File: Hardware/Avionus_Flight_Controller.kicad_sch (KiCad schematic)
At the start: 1 part

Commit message: More routing
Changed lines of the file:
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@@
       (effects (font (size 1.27 1.27)) (justify left))
     )
-    (pin "TIM4_CH2" output (at 127 154.94 180)
+    (pin "TIM4_CH2" output (at 127 157.48 180)
       (effects (font (size 1.27 1.27)) (justify left))
     )
@@
       (effects (font (size 1.27 1.27)) (justify left))
     )
-    (pin "TIM4_CH1" output (at 127 157.48 180)
+    (pin "TIM4_CH1" output (at 127 154.94 180)
       (effects (font (size 1.27 1.27)) (justify left))
     )

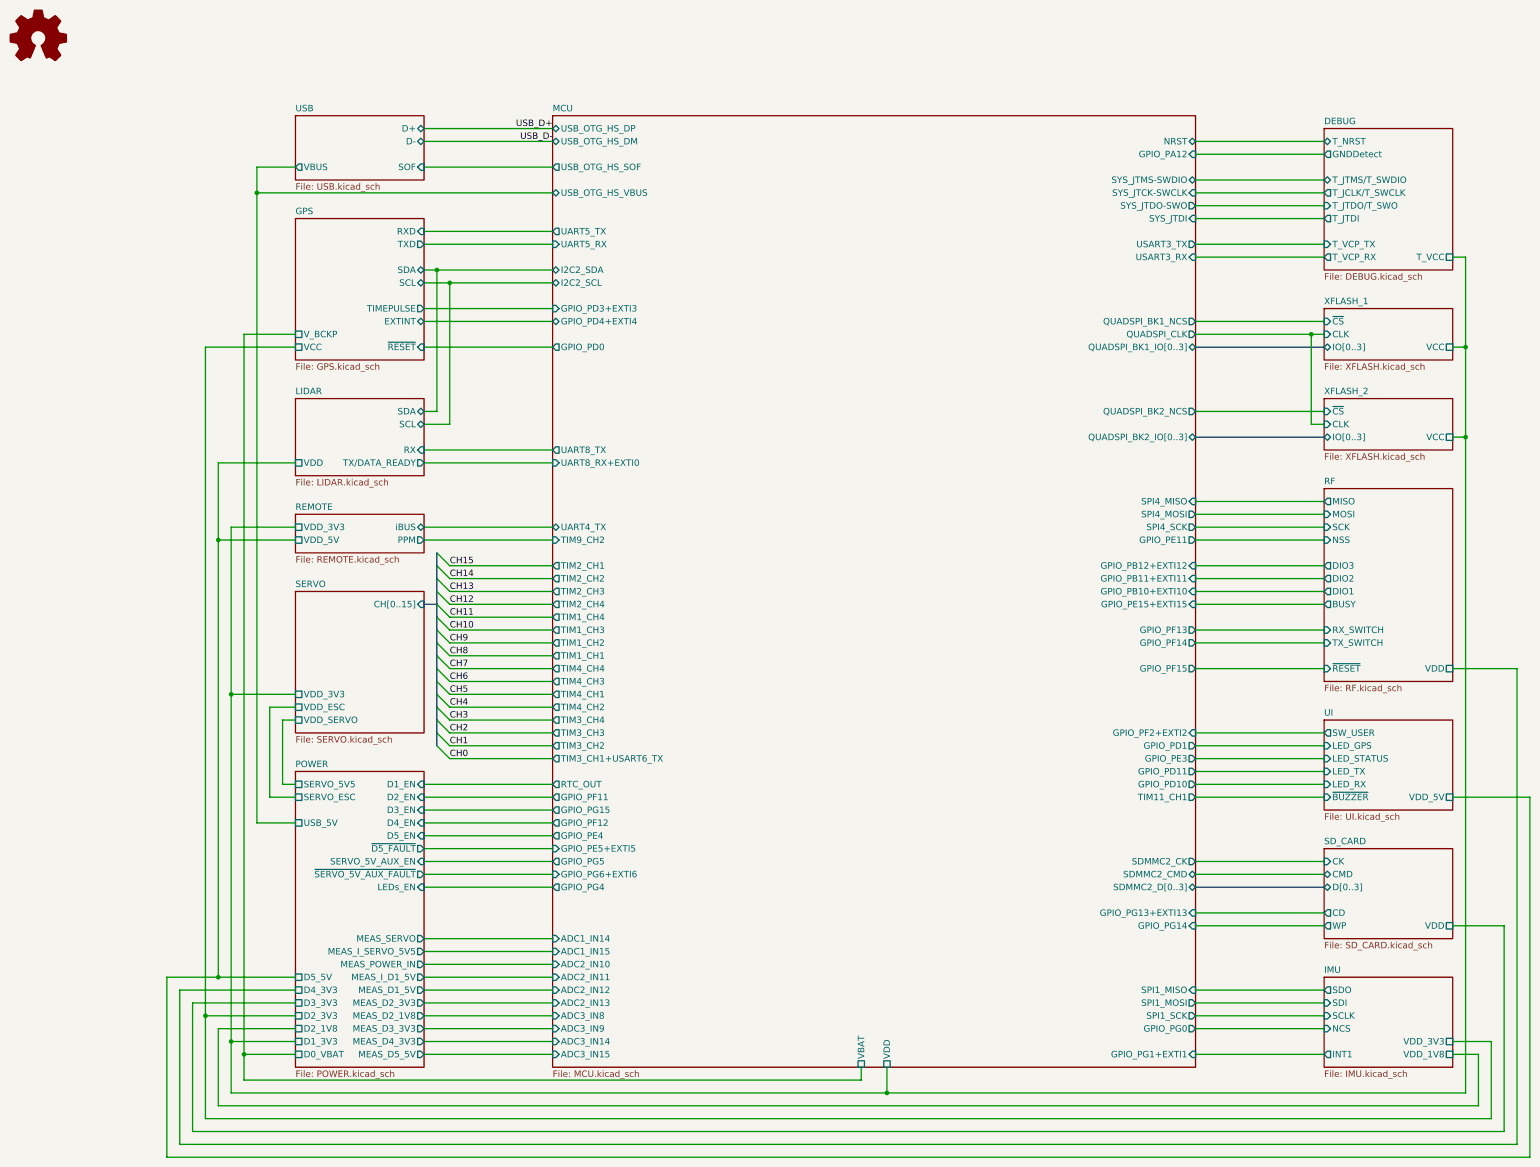
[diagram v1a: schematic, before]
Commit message: Schematic layout fixes
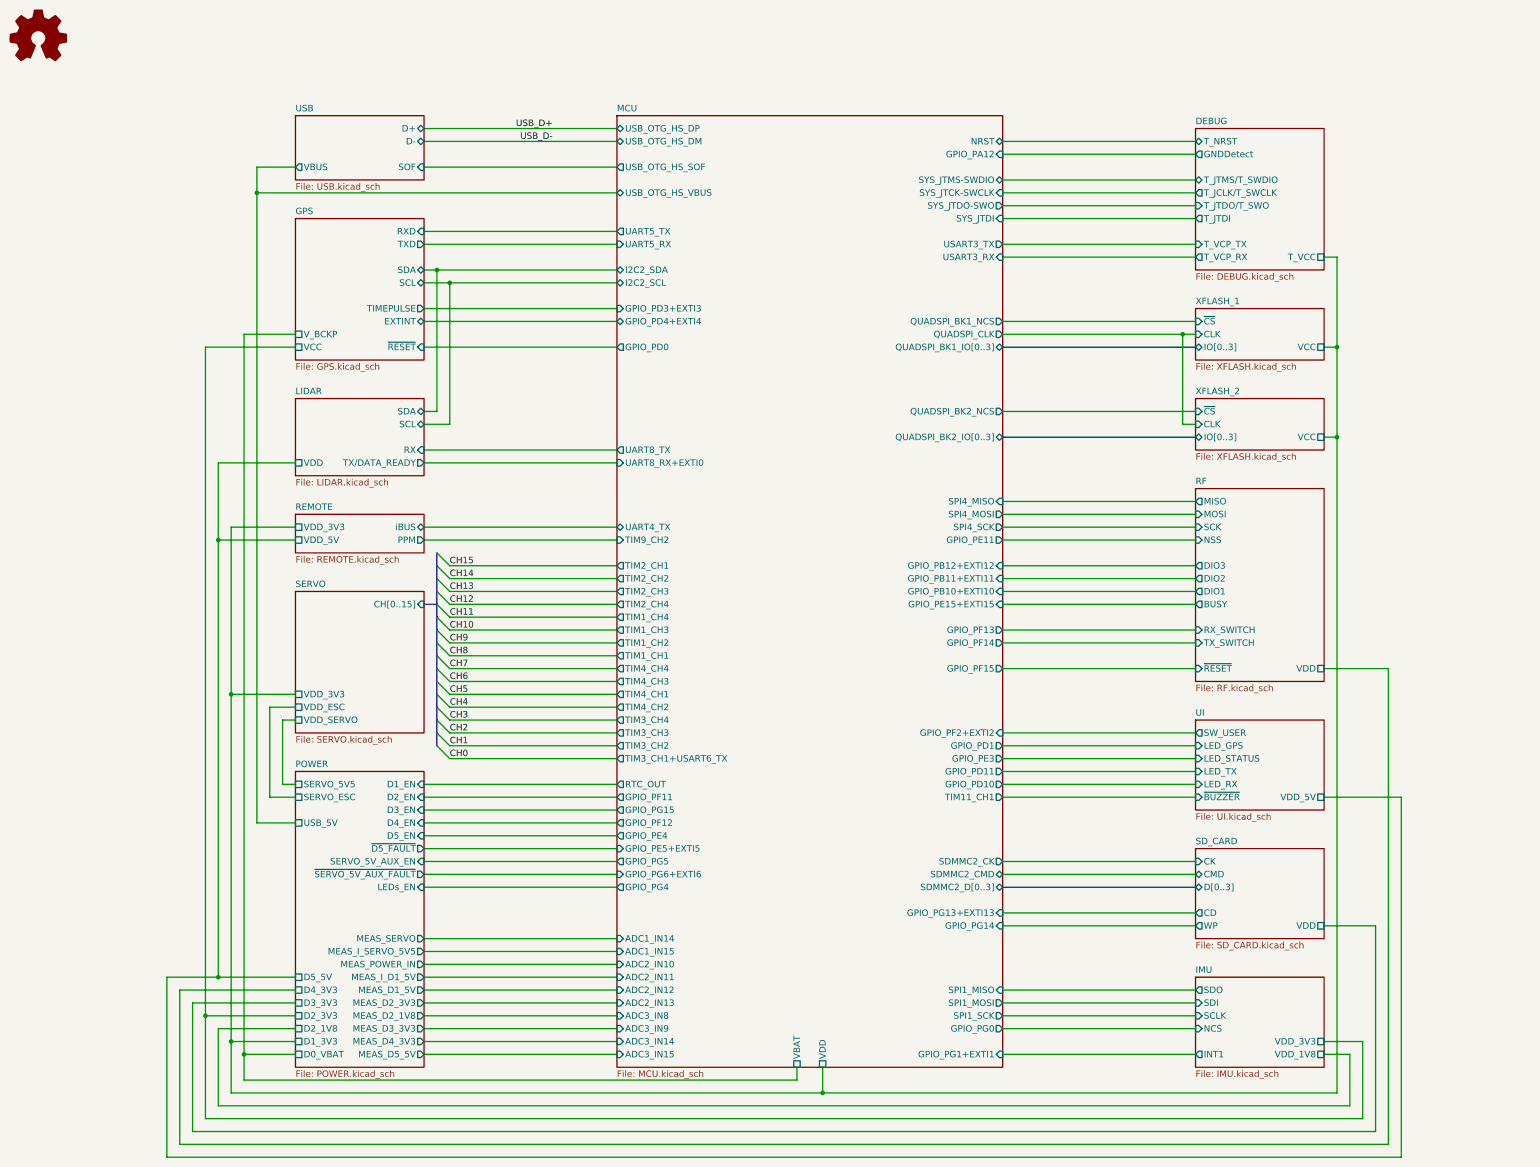
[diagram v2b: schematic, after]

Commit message: Misc fixes
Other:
- sheet MCU ports: added GPIO_PE2; removed GPIO_PD1
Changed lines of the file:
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@@
       (effects (font (size 1.27 1.27)) (justify left))
-    )
-    (pin "GPIO_PD1" output (at 215.9 165.1 0)
-      (effects (font (size 1.27 1.27)) (justify right))
     )
     (pin "GPIO_PD4+EXTI4" bidirectional (at 139.7 81.28 180)
@@
       (effects (font (size 1.27 1.27)) (justify right))
     )
+    (pin "GPIO_PE2" output (at 215.9 165.1 0)
+      (effects (font (size 1.27 1.27)) (justify right))
+    )

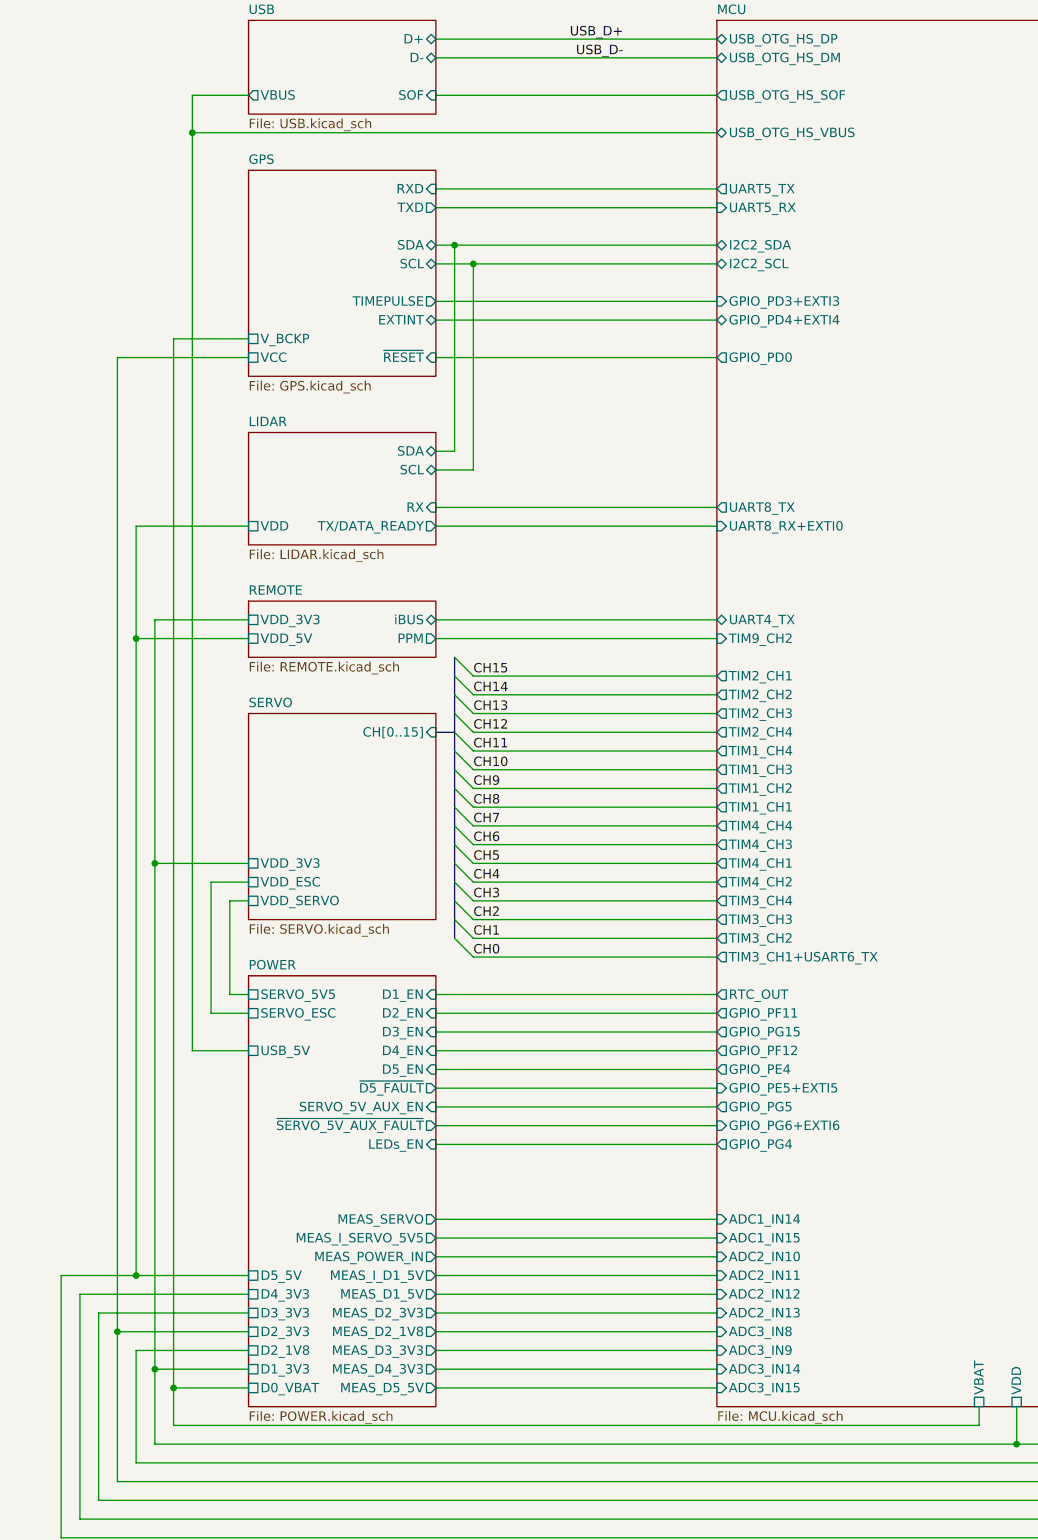
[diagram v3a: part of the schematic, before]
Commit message: Add lidar2
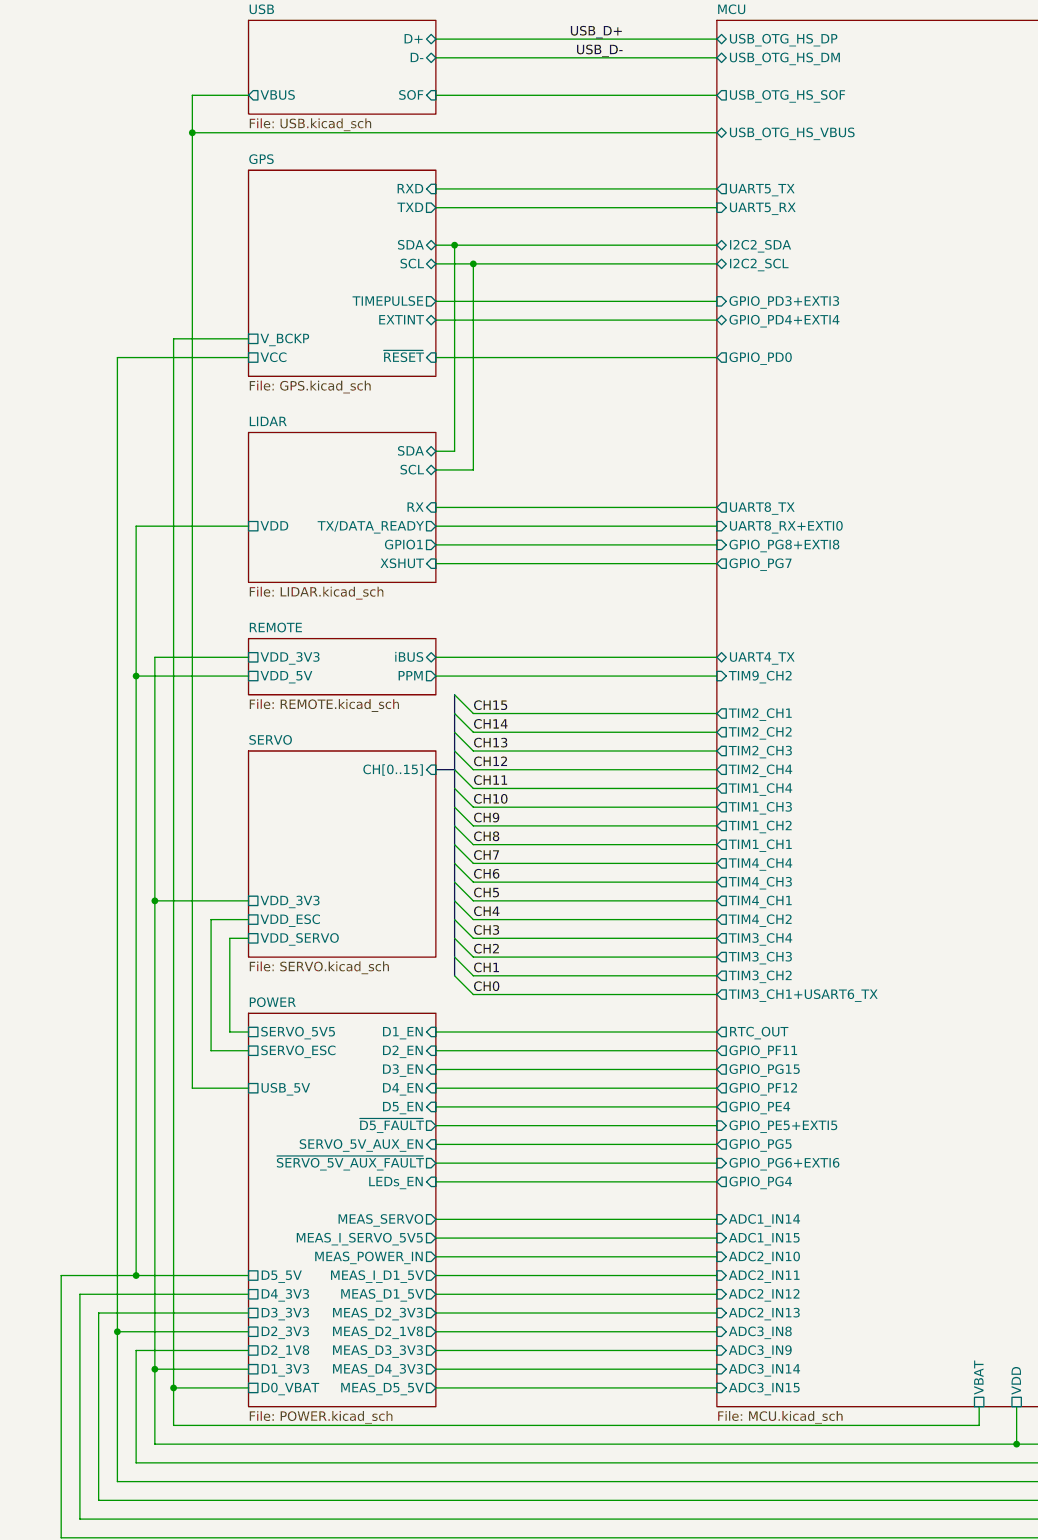
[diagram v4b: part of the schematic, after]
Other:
- sheet LIDAR ports: added GPIO1, XSHUT; removed none
- sheet MCU ports: added GPIO_PG7, GPIO_PG8+EXTI8; removed none

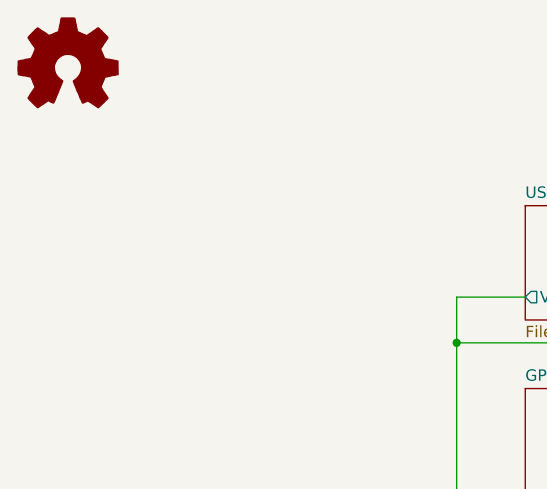
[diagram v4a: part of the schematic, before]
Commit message: Add mounting holes
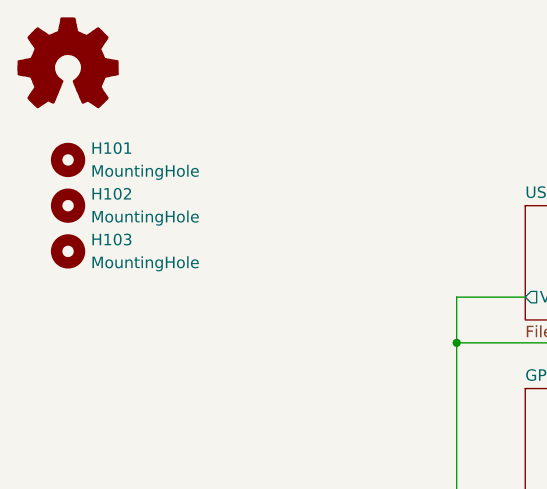
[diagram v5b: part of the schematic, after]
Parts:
- added H101, H102, H103: MountingHole, MountingHole:MountingHole_3.2mm_M3, symbol Mechanical:MountingHole
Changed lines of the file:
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@@
     (effects (font (size 1.27 1.27)) (justify left bottom))
+  )
+  (symbol (lib_id "Mechanical:MountingHole") (at 25.4 35.56 0) (unit 1)
+    (in_bom yes) (on_board yes) (dnp no) (fields_autoplaced)
+    (property "Reference" "H101" (at 27.94 34.29 0)
+      (effects (font (size 1.27 1.27)) (justify left))
+    )
+    (property "Value" "MountingHole" (at 27.94 36.83 0)
+      (effects (font (size 1.27 1.27)) (justify left))
+    )
+    (property "Footprint" "MountingHole:MountingHole_3.2mm_M3" (at 25.4 35.56 0)
+      (effects (font (size 1.27 1.27)) hide)
+    )
+    (property "Datasheet" "~" (at 25.4 35.56 0)
+      (effects (font (size 1.27 1.27)) hide)
+    )
+    (instances
+      (project "Avionus_Flight_Controller"
+        (path "/ddc7e940-0588-4587-8902-8ced9e615ace"
+          (reference "H101") (unit 1)
+        )
+      )
+    )
+  )
+  (symbol (lib_id "Mechanical:MountingHole") (at 25.4 45.72 0) (unit 1)
+    (in_bom yes) (on_board yes) (dnp no) (fields_autoplaced)
+    (property "Reference" "H103" (at 27.94 44.45 0)
+      (effects (font (size 1.27 1.27)) (justify left))
+    )
+    (property "Value" "MountingHole" (at 27.94 46.99 0)
+      (effects (font (size 1.27 1.27)) (justify left))
+    )
+    (property "Footprint" "MountingHole:MountingHole_3.2mm_M3" (at 25.4 45.72 0)
+      (effects (font (size 1.27 1.27)) hide)
+    )
+    (property "Datasheet" "~" (at 25.4 45.72 0)
+      (effects (font (size 1.27 1.27)) hide)
+    )
+    (instances
+      (project "Avionus_Flight_Controller"
+        (path "/ddc7e940-0588-4587-8902-8ced9e615ace"
+          (reference "H103") (unit 1)
+        )
+      )
+    )
   )
   (symbol (lib_id "Graphic:Logo_Open_Hardware_Small") (at 25.4 25.4 0) (unit 1)
@@
         )
       )
+    )
+  )
+  (symbol (lib_id "Mechanical:MountingHole") (at 25.4 40.64 0) (unit 1)
+    (in_bom yes) (on_board yes) (dnp no) (fields_autoplaced)
+    (property "Reference" "H102" (at 27.94 39.37 0)
+      (effects (font (size 1.27 1.27)) (justify left))
+    )
+    (property "Value" "MountingHole" (at 27.94 41.91 0)
+      (effects (font (size 1.27 1.27)) (justify left))
+    )
+    (property "Footprint" "MountingHole:MountingHole_3.2mm_M3" (at 25.4 40.64 0)
+      (effects (font (size 1.27 1.27)) hide)
+    )
+    (property "Datasheet" "~" (at 25.4 40.64 0)
+      (effects (font (size 1.27 1.27)) hide)
+    )
+    (instances
+      (project "Avionus_Flight_Controller"
+        (path "/ddc7e940-0588-4587-8902-8ced9e615ace"
+          (reference "H102") (unit 1)
+        )
+      )

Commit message: Finalize silkscreen
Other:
- title: (none) -> Avionus_Flight_Controller
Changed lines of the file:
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@@
 (kicad_sch (version 20230121) (generator eeschema)
   (paper "A3")
+  (title_block
+    (title "Avionus_Flight_Controller")
+    (date "2023-11-25")
+    (rev "1.0")
+  )
   (junction (at 63.5 160.02) (diameter 0) (color 0 0 0 0)
   )
